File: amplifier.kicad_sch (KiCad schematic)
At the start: 11 parts, among them U1 MAX9814

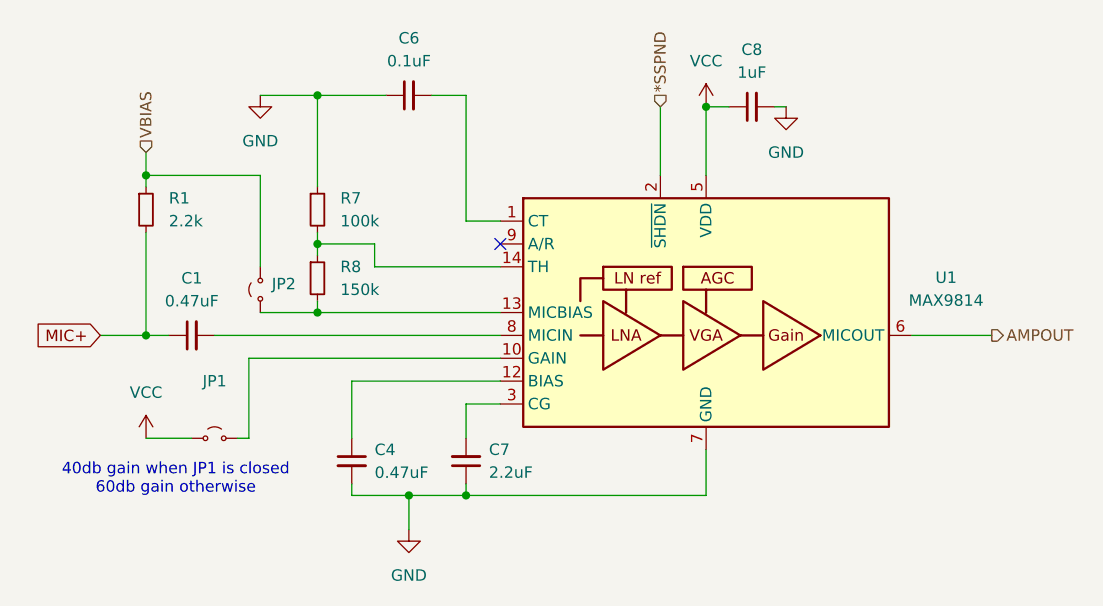
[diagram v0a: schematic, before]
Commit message: Added Connectors; added hierarchical labels connections
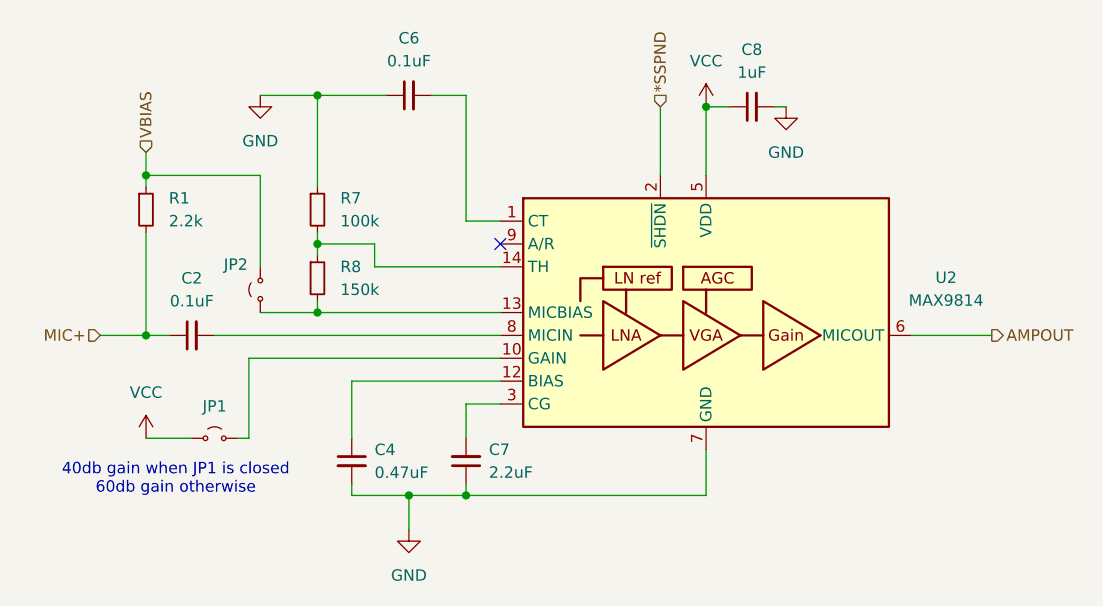
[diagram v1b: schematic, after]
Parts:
- C2: renamed from C1; value 0.47uF -> 0.1uF
- renumbered U1 to U2
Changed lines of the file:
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@@
-		)
-	)
-	(global_label "MIC+"
-		(shape input)
-		(at 124.46 115.57 180)
-		(fields_autoplaced yes)
-		(effects
-			(font
-				(size 1.27 1.27)
-			)
-			(justify right)
-		)
-		(property "Intersheetrefs" "${INTERSHEET_REFS}"
-			(at 116.5762 115.57 0)
-			(effects
-				(font
-					(size 1.27 1.27)
-				)
-				(justify right)
-				(hide yes)
-			)
 		)
 	)
@@
 		)
 	)
+	(hierarchical_label "MIC+"
+		(shape input)
+		(at 124.46 115.57 180)
+		(effects
+			(font
+				(size 1.27 1.27)
+			)
+			(justify right)
+		)
+	)
 	(hierarchical_label "AMPOUT"
 		(shape output)
@@
 		(dnp no)
 		(fields_autoplaced yes)
-		(property "Reference" "C1"
+		(property "Reference" "C2"
 			(at 134.6263 109.22 90)
 			(effects
@@
 			)
 		)
-		(property "Value" "0.47uF"
+		(property "Value" "0.1uF"
 			(at 134.6263 111.76 90)
 			(effects
@@
 			(project "lesson2"
 				(path "/eb1afd54-626c-4526-850f-b0511eb9dc59/aed31a99-faa8-4ba4-96c0-f97b18d51065"
-					(reference "C1")
+					(reference "C2")
 					(unit 1)
 				)
@@
 		(dnp no)
 		(fields_autoplaced yes)
-		(property "Reference" "U1"
+		(property "Reference" "U2"
 			(at 218.44 109.1498 0)
 			(effects
@@
 			(project ""
 				(path "/eb1afd54-626c-4526-850f-b0511eb9dc59/aed31a99-faa8-4ba4-96c0-f97b18d51065"
-					(reference "U1")
+					(reference "U2")
 					(unit 1)
 				)
@@
 		(on_board yes)
 		(dnp no)
-		(fields_autoplaced yes)
 		(property "Reference" "JP2"
-			(at 143.51 109.8549 90)
+			(at 138.176 107.696 90)
 			(effects
 				(font
@@
 		(on_board yes)
 		(dnp no)
-		(fields_autoplaced yes)
 		(property "Reference" "JP1"
-			(at 137.16 120.65 0)
-			(effects
-				(font
+			(at 137.16 123.444 0)
+			(effects
+				(font

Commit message: Add missing PCM2906 components; Partially Implement PCB
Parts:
- C1: renamed from C2; footprint (none) -> Capacitor_SMD:C_0603_1608Metric_Pad1.08x0.95mm_HandSolder
- C2: renamed from C4; footprint (none) -> Capacitor_SMD:C_0603_1608Metric_Pad1.08x0.95mm_HandSolder
- C3: renamed from C6; footprint (none) -> Capacitor_SMD:C_0603_1608Metric_Pad1.08x0.95mm_HandSolder
- C4: renamed from C7; footprint (none) -> Capacitor_SMD:C_0603_1608Metric_Pad1.08x0.95mm_HandSolder
- C5: renamed from C8; footprint (none) -> Capacitor_SMD:C_0603_1608Metric_Pad1.08x0.95mm_HandSolder
- JP1, JP2: footprint (none) -> Connector_PinHeader_1.27mm:PinHeader_1x02_P1.27mm_Vertical
- R1: footprint (none) -> Resistor_SMD:R_0603_1608Metric_Pad0.98x0.95mm_HandSolder
- R2: renamed from R7; footprint (none) -> Resistor_SMD:R_0603_1608Metric_Pad0.98x0.95mm_HandSolder
- R3: renamed from R8; footprint (none) -> Resistor_SMD:R_0603_1608Metric_Pad0.98x0.95mm_HandSolder
- renumbered U2 to U1
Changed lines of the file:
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@@
 		(dnp no)
 		(fields_autoplaced yes)
-		(property "Reference" "#PWR06"
+		(property "Reference" "#PWR01"
 			(at 129.54 130.81 0)
 			(effects
@@
 			(project "lesson2"
 				(path "/eb1afd54-626c-4526-850f-b0511eb9dc59/aed31a99-faa8-4ba4-96c0-f97b18d51065"
-					(reference "#PWR06")
+					(reference "#PWR01")
 					(unit 1)
 				)
@@
 		(dnp no)
 		(fields_autoplaced yes)
-		(property "Reference" "#PWR01"
+		(property "Reference" "#PWR04"
 			(at 191.77 93.98 0)
 			(effects
@@
 			(project ""
 				(path "/eb1afd54-626c-4526-850f-b0511eb9dc59/aed31a99-faa8-4ba4-96c0-f97b18d51065"
-					(reference "#PWR01")
+					(reference "#PWR04")
 					(unit 1)
 				)
@@
 		(dnp no)
 		(fields_autoplaced yes)
-		(property "Reference" "C2"
+		(property "Reference" "C1"
 			(at 134.6263 109.22 90)
 			(effects
@@
 			)
 		)
-		(property "Footprint" ""
+		(property "Footprint" "Capacitor_SMD:C_0603_1608Metric_Pad1.08x0.95mm_HandSolder"
 			(at 134.62 115.57 0)
 			(effects
@@
 			(project "lesson2"
 				(path "/eb1afd54-626c-4526-850f-b0511eb9dc59/aed31a99-faa8-4ba4-96c0-f97b18d51065"
-					(reference "C2")
+					(reference "C1")
 					(unit 1)
 				)
@@
 		(dnp no)
 		(fields_autoplaced yes)
-		(property "Reference" "#PWR03"
+		(property "Reference" "#PWR02"
 			(at 142.24 95.25 0)
 			(effects
@@
 			(project "lesson2"
 				(path "/eb1afd54-626c-4526-850f-b0511eb9dc59/aed31a99-faa8-4ba4-96c0-f97b18d51065"
-					(reference "#PWR03")
+					(reference "#PWR02")
 					(unit 1)
 				)
@@
 		(dnp no)
 		(fields_autoplaced yes)
-		(property "Reference" "#PWR05"
+		(property "Reference" "#PWR03"
 			(at 158.75 143.51 0)
 			(effects
@@
 			(project "lesson2"
 				(path "/eb1afd54-626c-4526-850f-b0511eb9dc59/aed31a99-faa8-4ba4-96c0-f97b18d51065"
-					(reference "#PWR05")
+					(reference "#PWR03")
 					(unit 1)
 				)
@@
 		(dnp no)
 		(fields_autoplaced yes)
-		(property "Reference" "U2"
+		(property "Reference" "U1"
 			(at 218.44 109.1498 0)
 			(effects
@@
 			(project ""
 				(path "/eb1afd54-626c-4526-850f-b0511eb9dc59/aed31a99-faa8-4ba4-96c0-f97b18d51065"
-					(reference "U2")
+					(reference "U1")
 					(unit 1)
 				)
@@
 		(dnp no)
 		(fields_autoplaced yes)
-		(property "Reference" "#PWR02"
+		(property "Reference" "#PWR05"
 			(at 200.66 96.52 0)
 			(effects
@@
 			(project ""
 				(path "/eb1afd54-626c-4526-850f-b0511eb9dc59/aed31a99-faa8-4ba4-96c0-f97b18d51065"
-					(reference "#PWR02")
+					(reference "#PWR05")
 					(unit 1)
 				)
@@
 			)
 		)
-		(property "Footprint" ""
+		(property "Footprint" "Connector_PinHeader_1.27mm:PinHeader_1x02_P1.27mm_Vertical"
 			(at 142.24 110.49 0)
 			(effects
@@
 		(dnp no)
 		(fields_autoplaced yes)
-		(property "Reference" "C4"
+		(property "Reference" "C2"
 			(at 154.94 128.2762 0)
 			(effects
@@
 			)
 		)
-		(property "Footprint" ""
+		(property "Footprint" "Capacitor_SMD:C_0603_1608Metric_Pad1.08x0.95mm_HandSolder"
 			(at 152.4 129.54 0)
 			(effects
@@
 			(project "lesson2"
 				(path "/eb1afd54-626c-4526-850f-b0511eb9dc59/aed31a99-faa8-4ba4-96c0-f97b18d51065"
-					(reference "C4")
+					(reference "C2")
 					(unit 1)
 				)
@@
 		(dnp no)
 		(fields_autoplaced yes)
-		(property "Reference" "R8"
+		(property "Reference" "R3"
 			(at 151.13 107.9499 0)
 			(effects
@@
 			)
 		)
-		(property "Footprint" ""
+		(property "Footprint" "Resistor_SMD:R_0603_1608Metric_Pad0.98x0.95mm_HandSolder"
 			(at 148.59 109.22 0)
 			(effects
@@
 			(project "lesson2"
 				(path "/eb1afd54-626c-4526-850f-b0511eb9dc59/aed31a99-faa8-4ba4-96c0-f97b18d51065"
-					(reference "R8")
+					(reference "R3")
 					(unit 1)
 				)
@@
 			)
 		)
-		(property "Footprint" ""
+		(property "Footprint" "Connector_PinHeader_1.27mm:PinHeader_1x02_P1.27mm_Vertical"
 			(at 137.16 127 0)
 			(effects
@@
 			)
 		)
-		(property "Footprint" ""
+		(property "Footprint" "Resistor_SMD:R_0603_1608Metric_Pad0.98x0.95mm_HandSolder"
 			(at 129.54 101.6 0)
 			(effects
@@
 		(dnp no)
 		(fields_autoplaced yes)
-		(property "Reference" "C6"
+		(property "Reference" "C3"
 			(at 158.7563 82.55 90)
 			(effects
@@
 			)
 		)
-		(property "Footprint" ""
+		(property "Footprint" "Capacitor_SMD:C_0603_1608Metric_Pad1.08x0.95mm_HandSolder"
 			(at 158.75 88.9 0)
 			(effects
@@
 			(project "lesson2"
 				(path "/eb1afd54-626c-4526-850f-b0511eb9dc59/aed31a99-faa8-4ba4-96c0-f97b18d51065"
-					(reference "C6")
+					(reference "C3")
 					(unit 1)
 				)
@@
 		(dnp no)
 		(fields_autoplaced yes)
-		(property "Reference" "R7"
+		(property "Reference" "R2"
 			(at 151.13 100.3299 0)
 			(effects
@@
 			)
 		)
-		(property "Footprint" ""
+		(property "Footprint" "Resistor_SMD:R_0603_1608Metric_Pad0.98x0.95mm_HandSolder"
 			(at 148.59 101.6 0)
 			(effects
@@
 			(project ""
 				(path "/eb1afd54-626c-4526-850f-b0511eb9dc59/aed31a99-faa8-4ba4-96c0-f97b18d51065"
-					(reference "R7")
+					(reference "R2")
 					(unit 1)
 				)
@@
 		(dnp no)
 		(fields_autoplaced yes)
-		(property "Reference" "C8"
+		(property "Reference" "C5"
 			(at 196.8563 83.82 90)
 			(effects
@@
 			)
 		)
-		(property "Footprint" ""
+		(property "Footprint" "Capacitor_SMD:C_0603_1608Metric_Pad1.08x0.95mm_HandSolder"
 			(at 196.85 90.17 0)
 			(effects
@@
 			(project ""
 				(path "/eb1afd54-626c-4526-850f-b0511eb9dc59/aed31a99-faa8-4ba4-96c0-f97b18d51065"
-					(reference "C8")
+					(reference "C5")
 					(unit 1)
 				)
@@
 		(dnp no)
 		(fields_autoplaced yes)
-		(property "Reference" "C7"
+		(property "Reference" "C4"
 			(at 167.64 128.2635 0)
 			(effects
@@
 			)
 		)
-		(property "Footprint" ""
+		(property "Footprint" "Capacitor_SMD:C_0603_1608Metric_Pad1.08x0.95mm_HandSolder"
 			(at 165.1 129.54 0)
 			(effects
@@
 			(project "lesson2"
 				(path "/eb1afd54-626c-4526-850f-b0511eb9dc59/aed31a99-faa8-4ba4-96c0-f97b18d51065"
-					(reference "C7")
-					(unit 1)
-				)
+					(reference "C4")
+					(unit 1)
+				)
